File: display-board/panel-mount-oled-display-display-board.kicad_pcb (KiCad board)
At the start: 2 copper layers, 40.7 x 21.1 mm, 2 parts, among them J1 Conn_01x08_Pin, J2 Conn_01x08_Pin

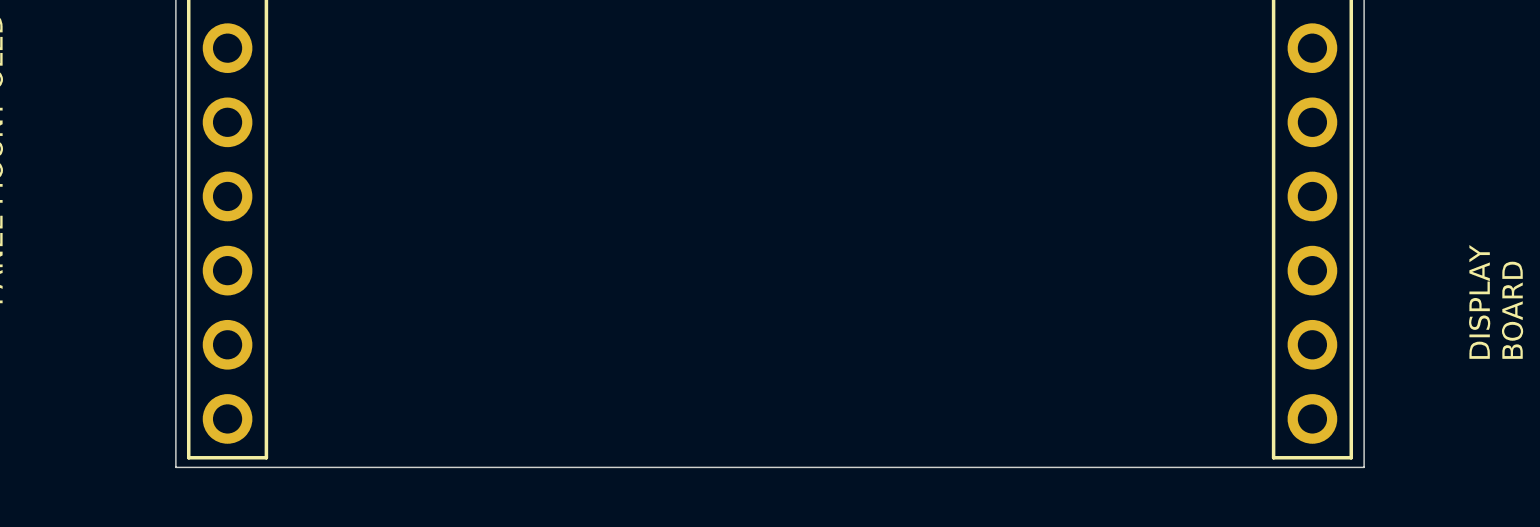
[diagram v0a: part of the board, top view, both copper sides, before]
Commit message: display: OLED handsolder footprint, schematic/PCB update, datasheets and backups
- Assign Display_Handsoldering OLED-128O064D_Handsoldering footprint and refresh board

- Update fp-lib-table and fp-info-cache

- Add datasheet PDFs, project backup zips, remove superseded connector backup
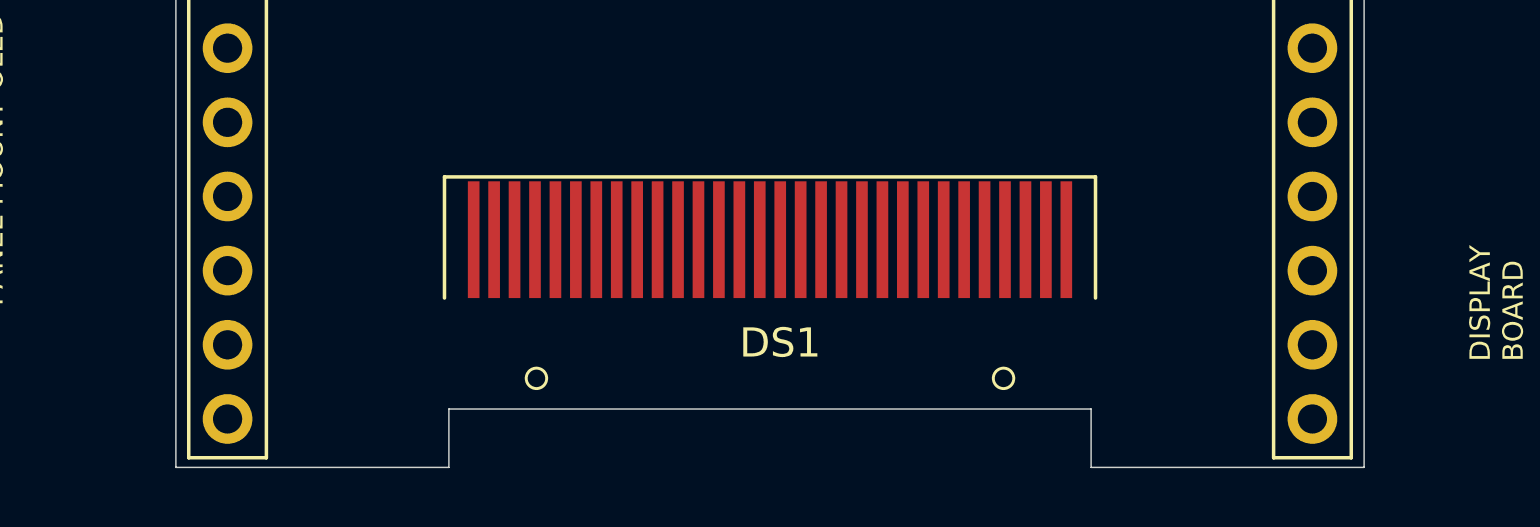
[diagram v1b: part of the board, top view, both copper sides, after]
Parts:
- added DS1: OLED-128O064D, Display_Handsoldering:OLED-128O064D_Handsoldering, F.Cu at (121.5, 114.3)
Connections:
- net /GND renamed GND
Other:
- outline, holes or cut-outs redrawn

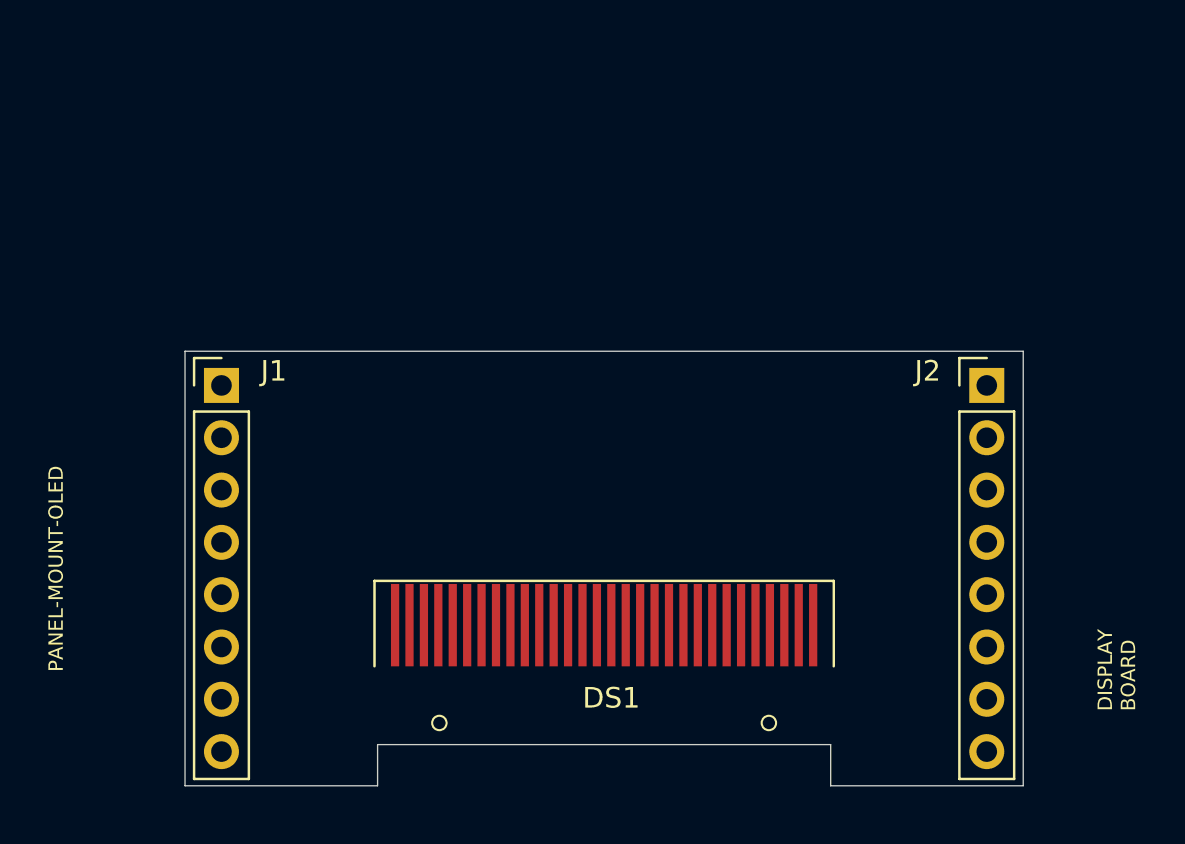
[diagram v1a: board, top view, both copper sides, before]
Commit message: Expand display board schematic with additional components
Update KiCad schematic and PCB to reflect new circuitry. Refresh
project backup archives and remove superseded backup snapshot.
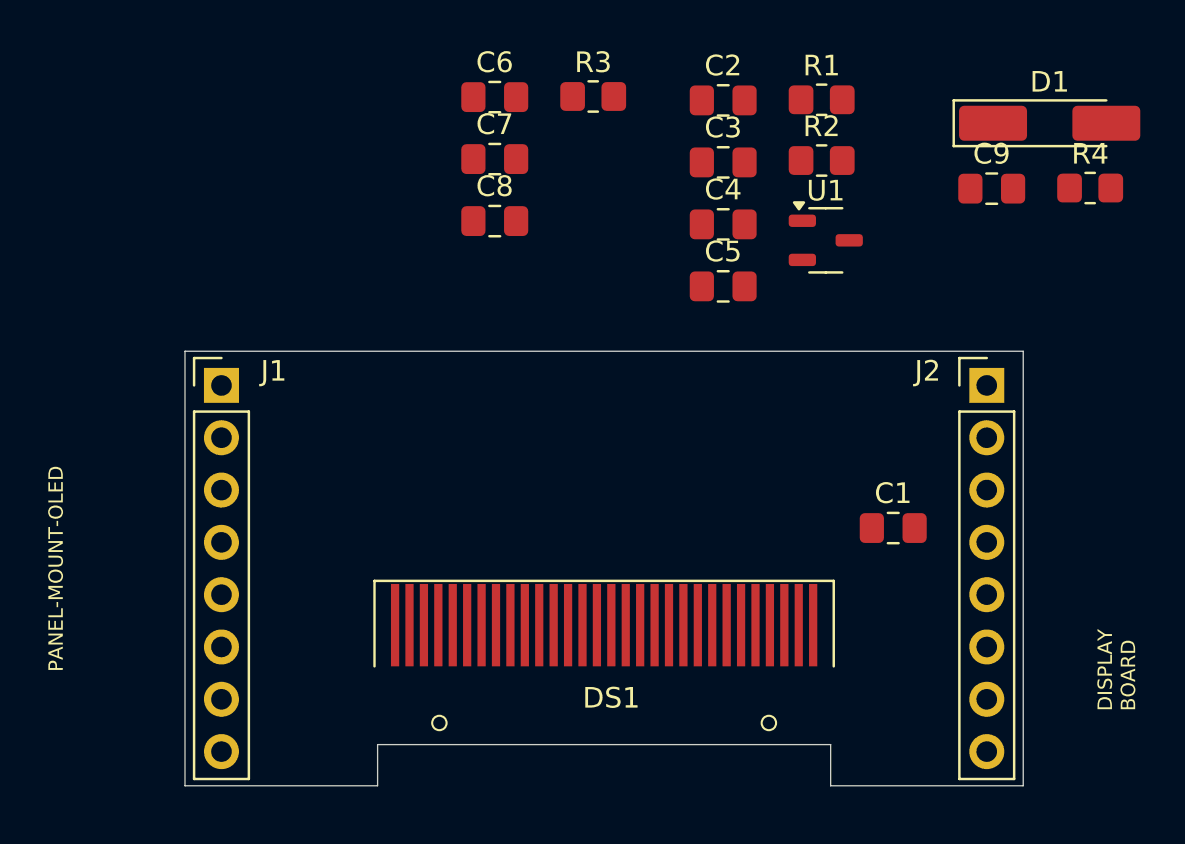
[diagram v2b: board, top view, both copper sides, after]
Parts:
- added C1: C, Capacitor_SMD:C_0805_2012Metric_Pad1.18x1.45mm_HandSolder, F.Cu at (135.5, 108.6)
- added C2: C, Capacitor_SMD:C_0805_2012Metric_Pad1.18x1.45mm_HandSolder, F.Cu at (127.2, 87.8)
- added C3: C, Capacitor_SMD:C_0805_2012Metric_Pad1.18x1.45mm_HandSolder, F.Cu at (127.2, 90.8)
- added C4: C, Capacitor_SMD:C_0805_2012Metric_Pad1.18x1.45mm_HandSolder, F.Cu at (127.2, 93.8)
- added C5: C, Capacitor_SMD:C_0805_2012Metric_Pad1.18x1.45mm_HandSolder, F.Cu at (127.2, 96.8)
- added C6: C, Capacitor_SMD:C_0805_2012Metric_Pad1.18x1.45mm_HandSolder, F.Cu at (116.1, 87.7)
- added C7: C, Capacitor_SMD:C_0805_2012Metric_Pad1.18x1.45mm_HandSolder, F.Cu at (116.1, 90.7)
- added C8: C, Capacitor_SMD:C_0805_2012Metric_Pad1.18x1.45mm_HandSolder, F.Cu at (116.1, 93.7)
- added C9: C, Capacitor_SMD:C_0805_2012Metric_Pad1.18x1.45mm_HandSolder, F.Cu at (140.3, 92.1)
- added D1: D, Diode_SMD:D_MiniMELF_Handsoldering, F.Cu at (143.1, 88.9)
- added R1: R, Resistor_SMD:R_0805_2012Metric_Pad1.20x1.40mm_HandSolder, F.Cu at (132.0, 87.8)
- added R2: R, Resistor_SMD:R_0805_2012Metric_Pad1.20x1.40mm_HandSolder, F.Cu at (132.0, 90.7)
- added R3: R, Resistor_SMD:R_0805_2012Metric_Pad1.20x1.40mm_HandSolder, F.Cu at (120.9, 87.6)
- added R4: R, Resistor_SMD:R_0805_2012Metric_Pad1.20x1.40mm_HandSolder, F.Cu at (145.1, 92.1)
- added U1: XC6206PxxxMR, Package_TO_SOT_SMD:SOT-23-3, F.Cu at (132.2, 94.6)
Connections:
- DS1 pad 1: Net-(DS1-GND-Pad1) -> GND
- DS1 pad 10: unconnected-(DS1-BS0-Pad10) -> GND
- DS1 pad 11: unconnected-(DS1-BS1-Pad11) -> /VCC
- DS1 pad 12: unconnected-(DS1-BS2-Pad12) -> GND
- DS1 pad 13: unconnected-(DS1-~{CS}-Pad13) -> GND
- DS1 pad 14: unconnected-(DS1-~{RES}-Pad14) -> Net-(D1-A)
- DS1 pad 15: unconnected-(DS1-D/~{C}-Pad15) -> GND
- DS1 pad 16: unconnected-(DS1-R/~{W}-Pad16) -> GND
- DS1 pad 17: unconnected-(DS1-E/~{RD}-Pad17) -> GND
- DS1 pad 18: unconnected-(DS1-D0-Pad18) -> /SCL
- DS1 pad 19: unconnected-(DS1-D1-Pad19) -> /SDA
- DS1 pad 2: unconnected-(DS1-C2N-Pad2) -> Net-(DS1-C2N)
- DS1 pad 20: unconnected-(DS1-D2-Pad20) -> /SDA
- DS1 pad 21: unconnected-(DS1-D3-Pad21) -> GND
- DS1 pad 22: unconnected-(DS1-D4-Pad22) -> GND
- DS1 pad 23: unconnected-(DS1-D5-Pad23) -> GND
- DS1 pad 24: unconnected-(DS1-D6-Pad24) -> GND
- DS1 pad 25: unconnected-(DS1-D7-Pad25) -> GND
- DS1 pad 26: unconnected-(DS1-IREF-Pad26) -> Net-(DS1-IREF)
- DS1 pad 27: unconnected-(DS1-VCOMH-Pad27) -> Net-(DS1-VCOMH)
- DS1 pad 28: unconnected-(DS1-VCC-Pad28) -> Net-(DS1-VCC)
- DS1 pad 29: unconnected-(DS1-VLSS-Pad29) -> GND
- DS1 pad 3: unconnected-(DS1-C2P-Pad3) -> Net-(DS1-C2P)
- DS1 pad 30: Net-(DS1-GND-Pad1) -> GND
- DS1 pad 4: unconnected-(DS1-C1P-Pad4) -> Net-(DS1-C1P)
- DS1 pad 5: unconnected-(DS1-C1N-Pad5) -> Net-(DS1-C1N)
- DS1 pad 6: unconnected-(DS1-VBAT-Pad6) -> Net-(DS1-VBAT)
- DS1 pad 8: unconnected-(DS1-VSS-Pad8) -> GND
- DS1 pad 9: unconnected-(DS1-VDD-Pad9) -> Net-(DS1-VBAT)

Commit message: display: finish board routing and checkpoint KiCad outputs
Capture the fully routed display board together with the generated KiCad
artifacts and fresh backups for this layout milestone.
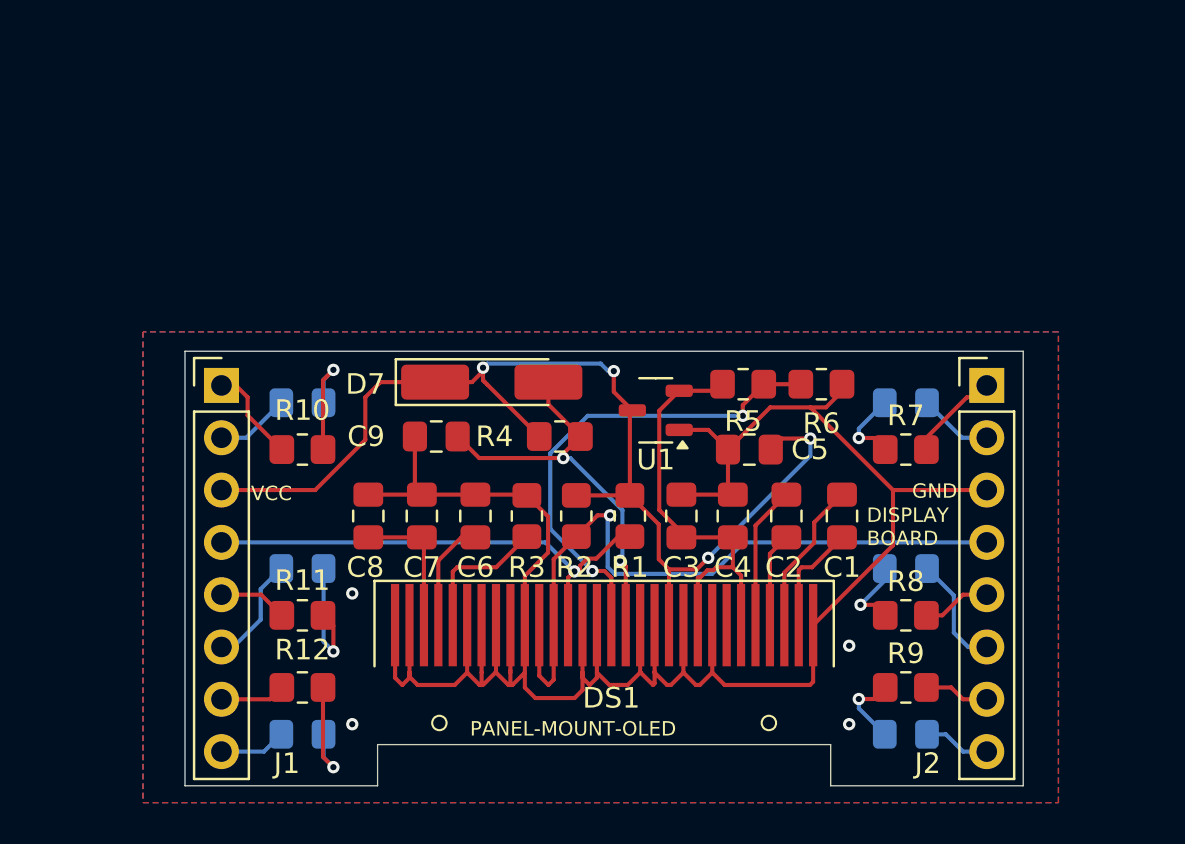
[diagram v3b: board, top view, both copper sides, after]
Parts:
- added D1: LED, LED_SMD:LED_0805_2012Metric_Pad1.15x1.40mm_HandSolder, B.Cu at (136.1, 102.5)
- added D2: LED, LED_SMD:LED_0805_2012Metric_Pad1.15x1.40mm_HandSolder, B.Cu at (136.1, 110.5)
- added D3: LED, LED_SMD:LED_0805_2012Metric_Pad1.15x1.40mm_HandSolder, B.Cu at (136.1, 118.6)
- added D4: LED, LED_SMD:LED_0805_2012Metric_Pad1.15x1.40mm_HandSolder, B.Cu at (106.8, 102.5)
- added D5: LED, LED_SMD:LED_0805_2012Metric_Pad1.15x1.40mm_HandSolder, B.Cu at (106.8, 110.5)
- added D6: LED, LED_SMD:LED_0805_2012Metric_Pad1.15x1.40mm_HandSolder, B.Cu at (106.8, 118.6)
- added R10: R, Resistor_SMD:R_0805_2012Metric_Pad1.20x1.40mm_HandSolder, F.Cu at (106.8, 104.8)
- added R11: R, Resistor_SMD:R_0805_2012Metric_Pad1.20x1.40mm_HandSolder, F.Cu at (106.8, 112.8)
- added R12: R, Resistor_SMD:R_0805_2012Metric_Pad1.20x1.40mm_HandSolder, F.Cu at (106.8, 116.3)
- added R5: R, Resistor_SMD:R_0805_2012Metric_Pad1.20x1.40mm_HandSolder, F.Cu at (128.2, 101.6)
- added R6: R, Resistor_SMD:R_0805_2012Metric_Pad1.20x1.40mm_HandSolder, F.Cu at (132.0, 101.6)
- added R7: R, Resistor_SMD:R_0805_2012Metric_Pad1.20x1.40mm_HandSolder, F.Cu at (136.1, 104.8)
- added R8: R, Resistor_SMD:R_0805_2012Metric_Pad1.20x1.40mm_HandSolder, F.Cu at (136.1, 112.8)
- added R9: R, Resistor_SMD:R_0805_2012Metric_Pad1.20x1.40mm_HandSolder, F.Cu at (136.1, 116.3)
- moved D7 29.9 mm to (116.0, 101.5)
- moved C9 29.5 mm to (113.3, 104.1)
- moved R4 28.4 mm to (119.3, 104.1)
- moved R1 22.3 mm to (122.7, 108.0), turned to -90 degrees
- moved R2 21.0 mm to (120.1, 108.0), turned to -90 degrees
- moved R3 20.6 mm to (117.7, 108.0), turned to 90 degrees
- moved C2 20.4 mm to (130.3, 108.0), turned to 90 degrees
- moved C6 20.4 mm to (115.2, 108.0), turned to -90 degrees
- moved C7 17.7 mm to (112.6, 108.0), turned to -90 degrees
- moved C3 17.3 mm to (125.2, 108.0), turned to -90 degrees
- moved C8 15.6 mm to (110.0, 108.0), turned to -90 degrees
- moved C4 14.2 mm to (127.7, 108.0), turned to -90 degrees
- moved U1 11.7 mm to (124.0, 102.9), turned to 180 degrees
- moved C5 8.03 mm to (128.5, 104.8)
- moved C1 2.56 mm to (133.0, 108.0), turned to 90 degrees
- renumbered D1 to D7
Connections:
- DS1 pad 15: GND -> Net-(DS1-D/~{C})
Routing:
- net GND: track 0.00 -> 112.7 mm, vias 0 -> 4
- net /VCC: track 0.00 -> 55.6 mm, vias 0 -> 4
- net /SDA: track 0.00 -> 35.3 mm, vias 0 -> 1
- net /SCL: track 0.00 -> 24.0 mm, vias 0 -> 1
- net Net-(DS1-D/~{C}): track 0.00 -> 23.8 mm, vias 0 -> 2
- net Net-(DS1-VBAT): track 0.00 -> 21.3 mm
- net Net-(D7-A): track 0.00 -> 21.1 mm, vias 0 -> 2
- net Net-(DS1-C2P): track 0.00 -> 7.50 mm
- net Net-(DS1-C1N): track 0.00 -> 6.96 mm
- net Net-(DS1-VCC): track 0.00 -> 6.90 mm
- net Net-(DS1-IREF): track 0.00 -> 6.90 mm
- net Net-(D5-K): track 0.00 -> 6.18 mm, vias 0 -> 1
- net Net-(D4-K): track 0.00 -> 5.87 mm, vias 0 -> 1
- net Net-(D6-K): track 0.00 -> 5.87 mm, vias 0 -> 1
- net /D2A: track 0.00 -> 5.54 mm
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- added copper zone on B.Cu, net GND
- added copper zone on F.Cu, net GND
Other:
- board text added: "GND"
- board text added: "PANEL MOUNT OLED"
- board text added: "VCC"
